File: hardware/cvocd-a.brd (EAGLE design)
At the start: 152.5 x 43.6 mm, 83 parts, among them IC1 PIC16F1825SO14, IC2 74HC595D, IC3 74HC595D, IC4 MCP4728_QUAD_DAC, IC5 LM324D, IC6 REG1117, IC7 6N138

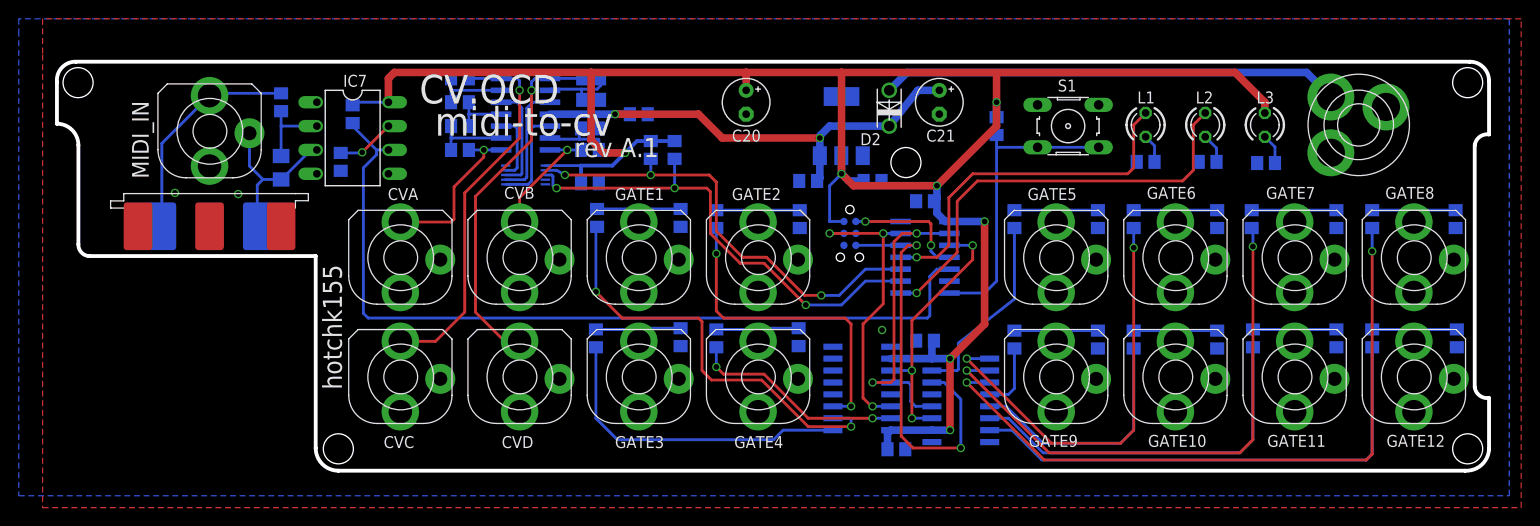
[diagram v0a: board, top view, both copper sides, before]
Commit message: smts moved to top of board
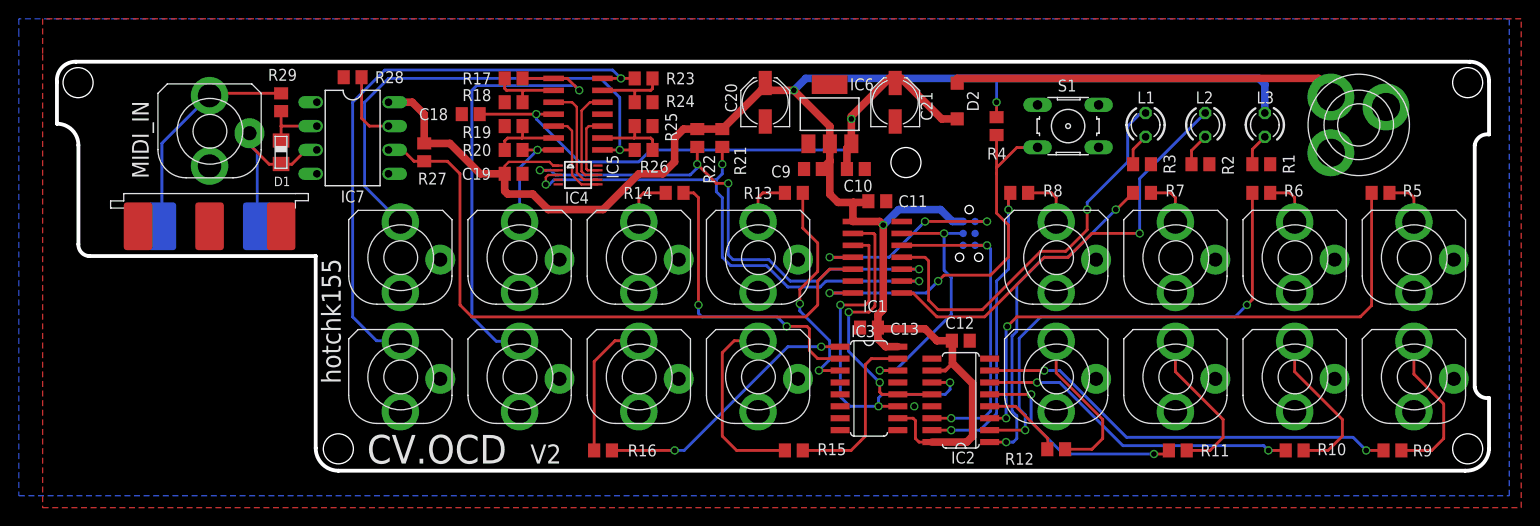
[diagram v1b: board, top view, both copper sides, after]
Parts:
- removed C1, C14, C15, C16, C17, C2, C3, C4, C5, C6, C7, C8: (no value), rcl:C0805
- C20, C21: device resistor:E2,5-5 -> rcl:PANASONIC_C
- D2: value 1N4004 -> (none); device jasons_stuff:DO-VERT -> diode:SOD123
- moved R23 19.6 mm to (62.7, 40.6), flipped to the top
- moved R24 19.6 mm to (62.7, 38.1), flipped to the top, turned to 180 degrees
- moved R25 19.6 mm to (62.7, 35.6), flipped to the top, turned to 180 degrees
- moved R26 19.6 mm to (62.7, 33.0), flipped to the top
- moved C18 17.9 mm to (44.3, 36.8), flipped to the top
- moved R15 14.5 mm to (78.7, 1.02), flipped to the top, turned to 180 degrees
- moved C13 13.3 mm to (86.7, 14.1), flipped to the top
- moved R10 12.7 mm to (132.1, 1.02), flipped to the top, turned to 0 degrees
- moved R11 12.7 mm to (119.6, 1.02), flipped to the top, turned to 0 degrees
- moved ICSP 12.7 mm to (97.4, 26.7)
- moved R12 12.5 mm to (106.7, 1.14), flipped to the top, turned to 0 degrees
- moved R9 12.1 mm to (142.5, 1.02), flipped to the top, turned to 0 degrees
- moved R16 12.0 mm to (58.4, 1.02), flipped to the top, turned to 180 degrees
- moved R28 9.11 mm to (31.8, 40.8), flipped to the top, turned to 180 degrees
- moved R13 8.72 mm to (78.7, 28.4), flipped to the top, turned to 180 degrees
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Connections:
- net GND: no longer C1.2, C14.2, C15.2, C16.2, C17.2, C2.2, C3.2, C4.2, C5.2, C6.2, C7.2, C8.2
- net N$1: no longer C16.1
- net N$20: no longer C4.1
- net N$23: no longer C3.1
- net N$24: no longer C2.1
- net N$32: no longer C1.1
- net N$33: no longer C8.1
- net N$39: no longer C7.1
- net N$41: no longer C6.1
- net N$52: no longer C5.1
- net N$6: no longer C17.1
- net N$7: no longer C15.1
- net N$8: no longer C14.1
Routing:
- net N$4: track 18.0 -> 52.4 mm
- net VDD: track 232.5 -> 204.4 mm, vias 7 -> 3
- net N$5: track 40.7 -> 62.8 mm
- net MIDI_IN: track 90.4 -> 68.6 mm
- net VIN: track 51.3 -> 69.5 mm
- net N$16: track 45.9 -> 32.5 mm
- net N$43: track 20.8 -> 31.7 mm, vias 0 -> 2
- net SR_CLK: track 28.0 -> 38.8 mm
- net N$1: track 9.86 -> 20.6 mm
- net N$2: track 38.5 -> 48.7 mm
- net N$47: track 73.4 -> 63.3 mm
- net N$15: track 34.5 -> 24.4 mm
- net N$46: track 46.1 -> 36.3 mm
- net N$9: track 32.3 -> 41.9 mm, vias 0 -> 2
- net SR_DAT2: track 43.9 -> 34.7 mm
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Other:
- board text added: "V2"
- board text removed: "midi-to-cv"
- board text removed: "rev A.1"
